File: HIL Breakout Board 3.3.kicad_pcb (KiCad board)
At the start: 4 copper layers, 262.5 x 26.2 mm, 4 parts, among them J1 DIN41612_03x32_C_Split, J2 DIN41612_03x32_C_Split, J3 HDRA-E68W1LFDT1EC+

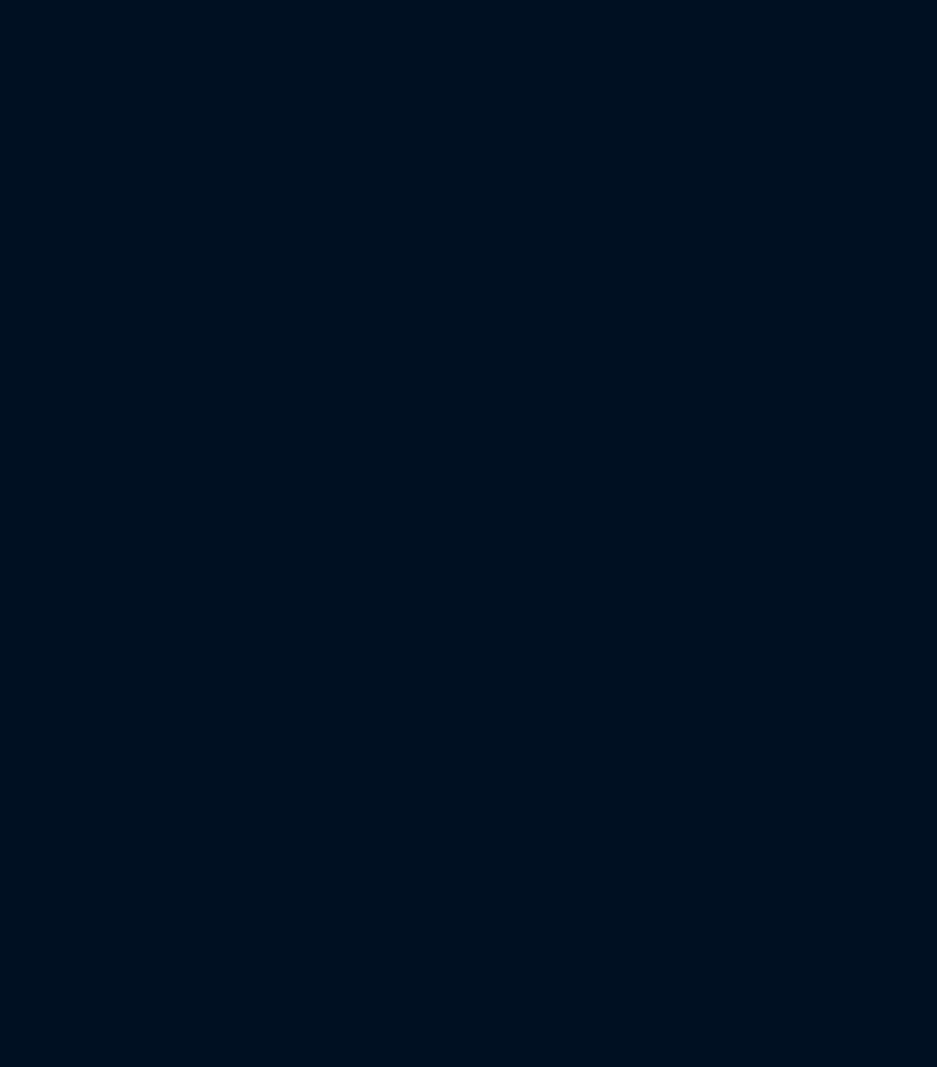
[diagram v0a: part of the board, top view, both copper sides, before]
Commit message: Added all analog inputs and outputs to schematic Schematic still missing +5 V on pin 1 and 35 and AISENSE1 on pin 56 for A and B side Updated PCB Design
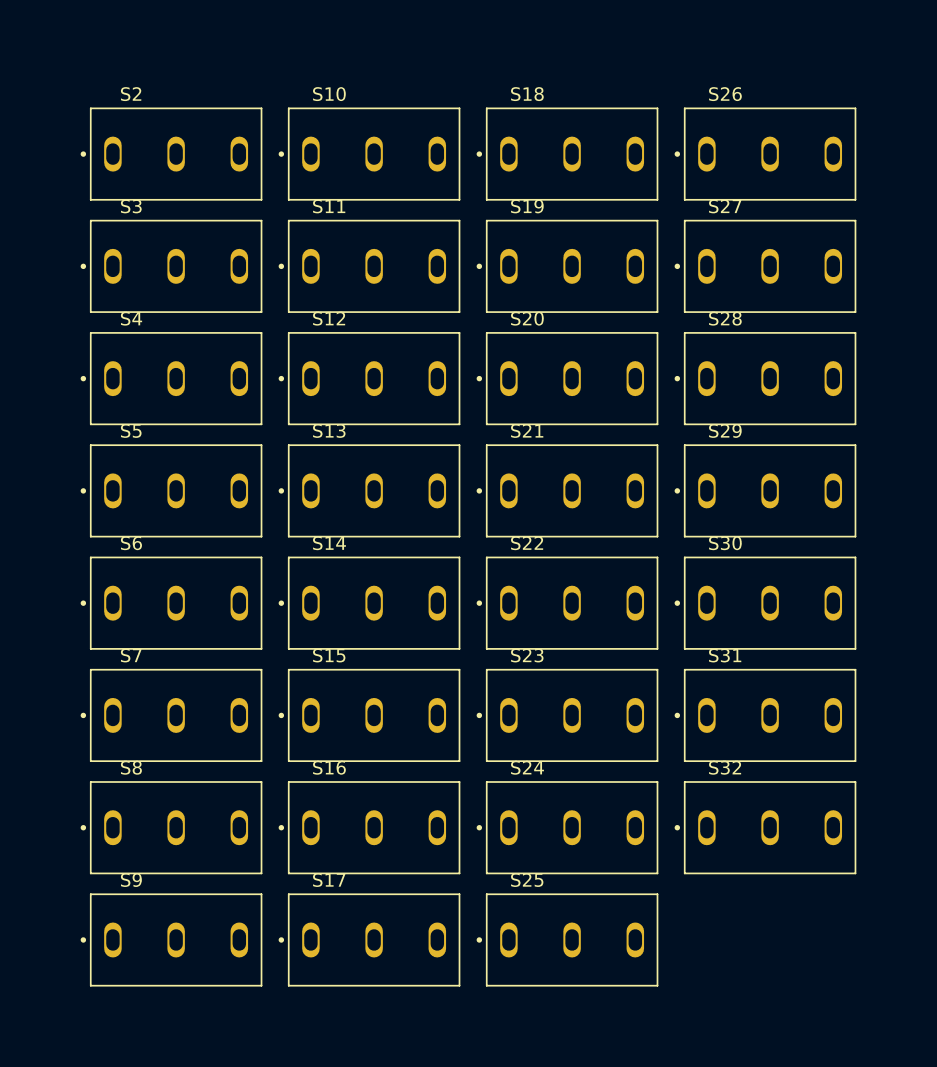
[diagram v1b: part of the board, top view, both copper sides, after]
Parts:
- added S10: SLW-1276864-4A-D, KiCad:SW_SLW-1276864-4A-D, F.Cu at (87.1, 74.3)
- added S11: SLW-1276864-4A-D, KiCad:SW_SLW-1276864-4A-D, F.Cu at (87.1, 82.6)
- added S12: SLW-1276864-4A-D, KiCad:SW_SLW-1276864-4A-D, F.Cu at (87.1, 91.0)
- added S13: SLW-1276864-4A-D, KiCad:SW_SLW-1276864-4A-D, F.Cu at (87.1, 99.3)
- added S14: SLW-1276864-4A-D, KiCad:SW_SLW-1276864-4A-D, F.Cu at (87.1, 107.7)
- added S15: SLW-1276864-4A-D, KiCad:SW_SLW-1276864-4A-D, F.Cu at (87.1, 116.0)
- added S16: SLW-1276864-4A-D, KiCad:SW_SLW-1276864-4A-D, F.Cu at (87.1, 124.4)
- added S17: SLW-1276864-4A-D, KiCad:SW_SLW-1276864-4A-D, F.Cu at (87.1, 132.7)
- added S18: SLW-1276864-4A-D, KiCad:SW_SLW-1276864-4A-D, F.Cu at (101.8, 74.3)
- added S19: SLW-1276864-4A-D, KiCad:SW_SLW-1276864-4A-D, F.Cu at (101.8, 82.6)
- added S2: SLW-1276864-4A-D, KiCad:SW_SLW-1276864-4A-D, F.Cu at (72.4, 74.3)
- added S20: SLW-1276864-4A-D, KiCad:SW_SLW-1276864-4A-D, F.Cu at (101.8, 91.0)
- added S21: SLW-1276864-4A-D, KiCad:SW_SLW-1276864-4A-D, F.Cu at (101.8, 99.3)
- added S22: SLW-1276864-4A-D, KiCad:SW_SLW-1276864-4A-D, F.Cu at (101.8, 107.7)
- added S23: SLW-1276864-4A-D, KiCad:SW_SLW-1276864-4A-D, F.Cu at (101.8, 116.0)
- added S24: SLW-1276864-4A-D, KiCad:SW_SLW-1276864-4A-D, F.Cu at (101.8, 124.4)
- added S25: SLW-1276864-4A-D, KiCad:SW_SLW-1276864-4A-D, F.Cu at (101.8, 132.7)
- added S26: SLW-1276864-4A-D, KiCad:SW_SLW-1276864-4A-D, F.Cu at (116.6, 74.3)
- added S27: SLW-1276864-4A-D, KiCad:SW_SLW-1276864-4A-D, F.Cu at (116.6, 82.6)
- added S28: SLW-1276864-4A-D, KiCad:SW_SLW-1276864-4A-D, F.Cu at (116.6, 91.0)
- added S29: SLW-1276864-4A-D, KiCad:SW_SLW-1276864-4A-D, F.Cu at (116.6, 99.3)
- added S3: SLW-1276864-4A-D, KiCad:SW_SLW-1276864-4A-D, F.Cu at (72.4, 82.6)
- added S30: SLW-1276864-4A-D, KiCad:SW_SLW-1276864-4A-D, F.Cu at (116.6, 107.7)
- added S31: SLW-1276864-4A-D, KiCad:SW_SLW-1276864-4A-D, F.Cu at (116.6, 116.0)
- added S32: SLW-1276864-4A-D, KiCad:SW_SLW-1276864-4A-D, F.Cu at (116.6, 124.4)
- added S4: SLW-1276864-4A-D, KiCad:SW_SLW-1276864-4A-D, F.Cu at (72.4, 91.0)
- added S5: SLW-1276864-4A-D, KiCad:SW_SLW-1276864-4A-D, F.Cu at (72.4, 99.3)
- added S6: SLW-1276864-4A-D, KiCad:SW_SLW-1276864-4A-D, F.Cu at (72.4, 107.7)
- added S7: SLW-1276864-4A-D, KiCad:SW_SLW-1276864-4A-D, F.Cu at (72.4, 116.0)
- added S8: SLW-1276864-4A-D, KiCad:SW_SLW-1276864-4A-D, F.Cu at (72.4, 124.4)
- added S9: SLW-1276864-4A-D, KiCad:SW_SLW-1276864-4A-D, F.Cu at (72.4, 132.7)
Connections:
- net ANO1 renamed AO0
- J1 pad a10: /ANout10 -> AO9
- J1 pad a11: /ANout11 -> AO10
- J1 pad a12: /ANout12 -> AO11
- J1 pad a13: /ANout13 -> AO12
- J1 pad a14: /ANout14 -> AO13
- J1 pad a15: unconnected-(J1A-Pin_a15-Pada15) -> AO14
- J1 pad a16: /ANout16 -> AO15
- J1 pad a2: /ANout2 -> AO1
- J1 pad a25: /ANin1 -> AI0
- J1 pad a26: /ANin2 -> AI1
- J1 pad a27: /ANin3 -> AI2
- J1 pad a28: /ANin4 -> AI3
- J1 pad a29: /ANin5 -> AI4
- J1 pad a3: /ANout3 -> AO2
- J1 pad a30: /ANin6 -> AI5
- J1 pad a31: /ANin7 -> AI6
- J1 pad a32: /ANin8 -> AI7
- J1 pad a4: /ANout4 -> AO3
- J1 pad a5: unconnected-(J1A-Pin_a5-Pada5) -> AO4
- J1 pad a6: /ANout6 -> AO5
- J1 pad a7: /ANout7 -> AO6
- J1 pad a8: /ANout8 -> AO7
- J1 pad a9: /ANout9 -> AO8
- J1 pad b25: /ANin9 -> AI8
- J1 pad b26: /ANin10 -> AI9
- J1 pad b27: /ANin11 -> AI10
- J1 pad b28: /ANin12 -> AI11
- J1 pad b29: /ANin13 -> AI12
- J1 pad b30: /ANin14 -> AI13
- J1 pad b31: /ANin15 -> AI14
- J1 pad b32: /ANin16 -> AI15
- J2 pad a1: /DI1 -> DI0
- J2 pad a10: /DI10 -> DI0
- J2 pad a11: /DI11 -> DI0
- J2 pad a12: /DI12 -> DI0
- J2 pad a13: /DI13 -> DI0
- J2 pad a14: /DI14 -> DI0
- J2 pad a15: /DI15 -> DI0
- J2 pad a16: /DI16 -> DI0
- J2 pad a17: /DI17 -> DI0
- J2 pad a18: /DI18 -> DI0
- J2 pad a19: /DI19 -> DI0
- J2 pad a2: /DI2 -> DI0
- J2 pad a20: /DI20 -> DI0
- J2 pad a21: /DI21 -> DI0
- J2 pad a22: /DI22 -> DI0
- J2 pad a23: /DI23 -> DI0
- J2 pad a24: /DI24 -> DI0
- J2 pad a25: /DI25 -> DI0
- J2 pad a26: /DI26 -> DI0
- J2 pad a27: /DI27 -> DI0
- J2 pad a28: /DI28 -> DI0
- J2 pad a29: /DI29 -> DI0
- J2 pad a3: /DI3 -> DI0
- J2 pad a30: /DI30 -> DI0
- J2 pad a31: /DI31 -> DI0
- J2 pad a32: /DI32 -> DI0
- J2 pad a4: /DI4 -> DI0
- J2 pad a5: /DI5 -> DI0
- J2 pad a6: /DI6 -> DI0
- J2 pad a7: /DI7 -> DI0
- J2 pad a8: /DI8 -> DI0
- J2 pad a9: /DI9 -> DI0
- J2 pad b1: /DO1 -> DO0
- J2 pad b10: /DO10 -> DO0
- J2 pad b11: /DO11 -> DO0
- J2 pad b12: /DO12 -> DO0
- J2 pad b13: /DO13 -> DO0
- J2 pad b14: /DO14 -> DO0
- J2 pad b15: /DO15 -> DO0
- J2 pad b16: /DO16 -> DO0
- J2 pad b17: /DO17 -> DO0
- J2 pad b18: /DO18 -> DO0
- J2 pad b19: /DO19 -> DO0
- J2 pad b2: /DO2 -> DO0
- J2 pad b20: /DO20 -> DO0
- J2 pad b21: /DO21 -> DO0
- J2 pad b22: /DO22 -> DO0
- J2 pad b23: /DO23 -> DO0
- J2 pad b24: /DO24 -> DO0
- J2 pad b25: /DO25 -> DO0
- J2 pad b26: /DO26 -> DO0
- J2 pad b27: /DO27 -> DO0
- J2 pad b28: /DO28 -> DO0
- J2 pad b29: /DO29 -> DO0
- J2 pad b3: /DO3 -> DO0
- J2 pad b30: /DO30 -> DO0
- J2 pad b31: /DO31 -> DO0
- J2 pad b32: /DO32 -> DO0
- J2 pad b4: /DO4 -> DO0
- J2 pad b5: /DO5 -> DO0
- J2 pad b6: /DO6 -> DO0
- J2 pad b7: /DO7 -> DO0
- J2 pad b8: /DO8 -> DO0
- J2 pad b9: /DO9 -> DO0
- J3 pad A10: unconnected-(J3-PadA10) -> Net-(J3-PadA10)
- J3 pad A11: unconnected-(J3-PadA11) -> Net-(J3-PadA11)
- J3 pad A12: unconnected-(J3-PadA12) -> Net-(J3-PadA12)
- J3 pad A13: unconnected-(J3-PadA13) -> Net-(J3-PadA13)
- J3 pad A14: unconnected-(J3-PadA14) -> AGND
- J3 pad A15: unconnected-(J3-PadA15) -> AGND
- J3 pad A16: unconnected-(J3-PadA16) -> AGND
- J3 pad A17: unconnected-(J3-PadA17) -> AGND
- J3 pad A18: unconnected-(J3-PadA18) -> AGND
- J3 pad A19: unconnected-(J3-PadA19) -> AGND
- J3 pad A2: unconnected-(J3-PadA2) -> DGND
- J3 pad A20: unconnected-(J3-PadA20) -> AGND
- J3 pad A21: unconnected-(J3-PadA21) -> AGND
- J3 pad A24: unconnected-(J3-PadA24) -> AGND
- J3 pad A27: unconnected-(J3-PadA27) -> AGND
- J3 pad A3: unconnected-(J3-PadA3) -> DGND
- J3 pad A30: unconnected-(J3-PadA30) -> AGND
- J3 pad A33: unconnected-(J3-PadA33) -> AGND
- J3 pad A37: unconnected-(J3-PadA37) -> Net-(J3-PadA37)
- J3 pad A38: unconnected-(J3-PadA38) -> Net-(J3-PadA38)
- J3 pad A39: unconnected-(J3-PadA39) -> Net-(J3-PadA39)
- J3 pad A4: unconnected-(J3-PadA4) -> DGND
- J3 pad A40: unconnected-(J3-PadA40) -> Net-(J3-PadA40)
- J3 pad A41: unconnected-(J3-PadA41) -> Net-(J3-PadA41)
- J3 pad A42: unconnected-(J3-PadA42) -> Net-(J3-PadA42)
- J3 pad A43: unconnected-(J3-PadA43) -> Net-(J3-PadA43)
- J3 pad A44: unconnected-(J3-PadA44) -> Net-(J3-PadA44)
- J3 pad A45: unconnected-(J3-PadA45) -> Net-(J3-PadA45)
- J3 pad A46: unconnected-(J3-PadA46) -> Net-(J3-PadA46)
- J3 pad A47: unconnected-(J3-PadA47) -> Net-(J3-PadA47)
- J3 pad A48: unconnected-(J3-PadA48) -> AI7
- J3 pad A49: unconnected-(J3-PadA49) -> AI6
- J3 pad A5: unconnected-(J3-PadA5) -> DGND
- J3 pad A50: unconnected-(J3-PadA50) -> AI5
- J3 pad A51: unconnected-(J3-PadA51) -> AI4
- J3 pad A52: unconnected-(J3-PadA52) -> AI3
- J3 pad A53: unconnected-(J3-PadA53) -> AI2
- J3 pad A54: unconnected-(J3-PadA54) -> AI1
- J3 pad A55: unconnected-(J3-PadA55) -> AI0
- J3 pad A57: unconnected-(J3-PadA57) -> AO7
- J3 pad A58: unconnected-(J3-PadA58) -> AGND
- J3 pad A59: unconnected-(J3-PadA59) -> AO6
- J3 pad A6: unconnected-(J3-PadA6) -> DGND
- J3 pad A60: unconnected-(J3-PadA60) -> AO5
- J3 pad A61: unconnected-(J3-PadA61) -> AGND
- J3 pad A62: unconnected-(J3-PadA62) -> AO4
- J3 pad A63: unconnected-(J3-PadA63) -> AO3
- J3 pad A64: unconnected-(J3-PadA64) -> AGND
- J3 pad A65: unconnected-(J3-PadA65) -> AO2
- J3 pad A66: unconnected-(J3-PadA66) -> AO1
- J3 pad A7: unconnected-(J3-PadA7) -> DGND
- J3 pad A8: unconnected-(J3-PadA8) -> DGND
- J3 pad A9: unconnected-(J3-PadA9) -> DGND
- J3 pad B10: unconnected-(J3-PadB10) -> Net-(J3-PadB10)
- J3 pad B11: unconnected-(J3-PadB11) -> Net-(J3-PadB11)
- J3 pad B12: unconnected-(J3-PadB12) -> Net-(J3-PadB12)
- J3 pad B13: unconnected-(J3-PadB13) -> Net-(J3-PadB13)
- J3 pad B14: unconnected-(J3-PadB14) -> AGND
- J3 pad B15: unconnected-(J3-PadB15) -> AGND
- J3 pad B16: unconnected-(J3-PadB16) -> AGND
- J3 pad B17: unconnected-(J3-PadB17) -> AGND
- J3 pad B18: unconnected-(J3-PadB18) -> AGND
- J3 pad B19: unconnected-(J3-PadB19) -> AGND
- J3 pad B2: unconnected-(J3-PadB2) -> DGND
- J3 pad B20: unconnected-(J3-PadB20) -> AGND
- J3 pad B21: unconnected-(J3-PadB21) -> AGND
- J3 pad B24: unconnected-(J3-PadB24) -> AGND
- J3 pad B27: unconnected-(J3-PadB27) -> AGND
- J3 pad B3: unconnected-(J3-PadB3) -> DGND
- J3 pad B30: unconnected-(J3-PadB30) -> AGND
- J3 pad B33: unconnected-(J3-PadB33) -> AGND
- J3 pad B36: unconnected-(J3-PadB36) -> Net-(J3-PadB36)
- J3 pad B37: unconnected-(J3-PadB37) -> Net-(J3-PadB37)
- J3 pad B38: unconnected-(J3-PadB38) -> Net-(J3-PadB38)
- J3 pad B39: unconnected-(J3-PadB39) -> Net-(J3-PadB39)
- J3 pad B4: unconnected-(J3-PadB4) -> DGND
- J3 pad B40: unconnected-(J3-PadB40) -> Net-(J3-PadB40)
- J3 pad B41: unconnected-(J3-PadB41) -> Net-(J3-PadB41)
- J3 pad B42: unconnected-(J3-PadB42) -> Net-(J3-PadB42)
- J3 pad B43: unconnected-(J3-PadB43) -> Net-(J3-PadB43)
- J3 pad B44: unconnected-(J3-PadB44) -> Net-(J3-PadB44)
- J3 pad B45: unconnected-(J3-PadB45) -> Net-(J3-PadB45)
- J3 pad B46: unconnected-(J3-PadB46) -> Net-(J3-PadB46)
- J3 pad B47: unconnected-(J3-PadB47) -> Net-(J3-PadB47)
- J3 pad B48: unconnected-(J3-PadB48) -> AI15
- J3 pad B49: unconnected-(J3-PadB49) -> AI14
- J3 pad B5: unconnected-(J3-PadB5) -> DGND
- J3 pad B50: unconnected-(J3-PadB50) -> AI13
- J3 pad B51: unconnected-(J3-PadB51) -> AI12
- J3 pad B52: unconnected-(J3-PadB52) -> AI11
- J3 pad B53: unconnected-(J3-PadB53) -> AI10
- J3 pad B54: unconnected-(J3-PadB54) -> AI9
- J3 pad B55: unconnected-(J3-PadB55) -> AI8
- J3 pad B57: unconnected-(J3-PadB57) -> AO15
- J3 pad B58: unconnected-(J3-PadB58) -> AGND
- J3 pad B59: unconnected-(J3-PadB59) -> AO14
- J3 pad B6: unconnected-(J3-PadB6) -> DGND
- J3 pad B60: unconnected-(J3-PadB60) -> AO13
- J3 pad B61: unconnected-(J3-PadB61) -> AGND
- J3 pad B62: unconnected-(J3-PadB62) -> AO12
- J3 pad B63: unconnected-(J3-PadB63) -> AO11
- J3 pad B64: unconnected-(J3-PadB64) -> AGND
- J3 pad B65: unconnected-(J3-PadB65) -> AO10
- J3 pad B66: unconnected-(J3-PadB66) -> AO9
- J3 pad B67: unconnected-(J3-PadB67) -> AGND
- J3 pad B68: unconnected-(J3-PadB68) -> AO8
- J3 pad B7: unconnected-(J3-PadB7) -> DGND
- J3 pad B8: unconnected-(J3-PadB8) -> DGND
- J3 pad B9: unconnected-(J3-PadB9) -> DGND
- S1 pad 1: /DI1 -> DI0
- S1 pad 3: /DO1 -> DO0

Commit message: Fixed the issue with naming of net labels so that all digital pins were not tied together
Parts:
- moved S32 162.0 mm to (277.9, 109.1), turned to 90 degrees
- moved S31 153.1 mm to (269.5, 109.1), turned to 90 degrees
- moved S30 144.6 mm to (261.2, 109.1), turned to 90 degrees
- moved S29 136.6 mm to (252.8, 109.1), turned to 90 degrees
- moved S28 129.2 mm to (244.5, 109.1), turned to 90 degrees
- moved S1 124.1 mm to (20.3, 109.1)
- moved S27 122.4 mm to (236.1, 109.1), turned to 90 degrees
- moved S25 120.2 mm to (219.7, 109.1), turned to 90 degrees
- moved S26 116.5 mm to (227.8, 109.1), turned to 90 degrees
- moved S24 110.6 mm to (211.4, 109.1), turned to 90 degrees
- moved S23 101.4 mm to (203.0, 109.1), turned to 90 degrees
- moved S22 92.8 mm to (194.7, 109.1), turned to 90 degrees
- moved S21 85.0 mm to (186.3, 109.1), turned to 90 degrees
- moved S20 78.2 mm to (178.0, 109.1), turned to 90 degrees
- moved S19 72.8 mm to (169.6, 109.1), turned to 90 degrees
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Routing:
- net AO0: track 222.5 -> 0.00 mm, vias 2 -> 0

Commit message: Got rid of all names of wires because it was causing issues with global variables Started PCB tracks
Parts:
- moved S1 169.0 mm to (184.8, 70.4), turned to 0 degrees
- moved S2 159.1 mm to (184.8, 80.5), turned to 0 degrees
- moved S3 149.3 mm to (184.8, 90.7), turned to 0 degrees
- moved S4 140.0 mm to (184.8, 100.8), turned to 0 degrees
- moved S5 131.5 mm to (184.8, 111.0), turned to 0 degrees
- moved S9 124.5 mm to (205.0, 70.4), turned to 0 degrees
- moved S6 123.7 mm to (184.8, 121.1), turned to 0 degrees
- moved S7 116.9 mm to (184.8, 131.2), turned to 0 degrees
- moved S10 113.9 mm to (205.1, 80.5), turned to 0 degrees
- moved S8 111.2 mm to (184.8, 141.4), turned to 0 degrees
- moved S11 103.6 mm to (205.1, 90.7), turned to 0 degrees
- moved S12 93.9 mm to (205.1, 100.8), turned to 0 degrees
- moved S13 85.2 mm to (205.0, 111.0), turned to 0 degrees
- moved S17 82.1 mm to (225.8, 70.4), turned to 0 degrees
- moved S14 78.0 mm to (205.2, 121.1), turned to 0 degrees
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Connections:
- J2 pad a10: DI0 -> DI9
- J2 pad a11: DI0 -> DI10
- J2 pad a12: DI0 -> DI11
- J2 pad a13: DI0 -> DI12
- J2 pad a14: DI0 -> DI13
- J2 pad a15: DI0 -> DI14
- J2 pad a16: DI0 -> DI15
- J2 pad a17: DI0 -> DI16
- J2 pad a18: DI0 -> DI17
- J2 pad a19: DI0 -> DI18
- J2 pad a2: DI0 -> DI1
- J2 pad a20: DI0 -> DI19
- J2 pad a21: DI0 -> DI20
- J2 pad a22: DI0 -> DI21
- J2 pad a23: DI0 -> DI22
- J2 pad a24: DI0 -> DI23
- J2 pad a25: DI0 -> DI24
- J2 pad a26: DI0 -> DI25
- J2 pad a27: DI0 -> DI26
- J2 pad a28: DI0 -> DI27
- J2 pad a29: DI0 -> DI28
- J2 pad a3: DI0 -> DI2
- J2 pad a30: DI0 -> DI29
- J2 pad a31: DI0 -> DI30
- J2 pad a32: DI0 -> DI31
- J2 pad a4: DI0 -> DI3
- J2 pad a5: DI0 -> DI4
- J2 pad a6: DI0 -> DI5
- J2 pad a7: DI0 -> DI6
- J2 pad a8: DI0 -> DI7
- J2 pad a9: DI0 -> DI8
- J2 pad b10: DO0 -> DO9
- J2 pad b11: DO0 -> DO10
- J2 pad b12: DO0 -> DO11
- J2 pad b13: DO0 -> DO12
- J2 pad b14: DO0 -> DO13
- J2 pad b15: DO0 -> DO14
- J2 pad b16: DO0 -> DO15
- J2 pad b17: DO0 -> DO16
- J2 pad b18: DO0 -> DO17
- J2 pad b19: DO0 -> DO18
- J2 pad b2: DO0 -> DO1
- J2 pad b20: DO0 -> DO19
- J2 pad b21: DO0 -> DO20
- J2 pad b22: DO0 -> DO21
- J2 pad b23: DO0 -> DO22
- J2 pad b24: DO0 -> DO23
- J2 pad b25: DO0 -> DO24
- J2 pad b26: DO0 -> DO25
- J2 pad b27: DO0 -> DO26
- J2 pad b28: DO0 -> DO27
- J2 pad b29: DO0 -> DO28
- J2 pad b3: DO0 -> DO2
- J2 pad b30: DO0 -> DO29
- J2 pad b31: DO0 -> DO30
- J2 pad b32: DO0 -> DO31
- J2 pad b4: DO0 -> DO3
- J2 pad b5: DO0 -> DO4
- J2 pad b6: DO0 -> DO5
- J2 pad b7: DO0 -> DO6
- J2 pad b8: DO0 -> DO7
- J2 pad b9: DO0 -> DO8
- S10 pad 1: DI0 -> DI9
- S10 pad 3: DO0 -> DO9
- S11 pad 1: DI0 -> DI10
- S11 pad 3: DO0 -> DO10
- S12 pad 1: DI0 -> DI11
- S12 pad 3: DO0 -> DO11
- S13 pad 1: DI0 -> DI12
- S13 pad 3: DO0 -> DO12
- S14 pad 1: DI0 -> DI13
- S14 pad 3: DO0 -> DO13
- S15 pad 1: DI0 -> DI14
- S15 pad 3: DO0 -> DO14
- S16 pad 1: DI0 -> DI15
- S16 pad 3: DO0 -> DO15
- S17 pad 1: DI0 -> DI16
- S17 pad 3: DO0 -> DO16
- S18 pad 1: DI0 -> DI17
- S18 pad 3: DO0 -> DO17
- S19 pad 1: DI0 -> DI18
- S19 pad 3: DO0 -> DO18
- S2 pad 1: DI0 -> DI1
- S2 pad 3: DO0 -> DO1
- S20 pad 1: DI0 -> DI19
- S20 pad 3: DO0 -> DO19
- S21 pad 1: DI0 -> DI20
- S21 pad 3: DO0 -> DO20
- S22 pad 1: DI0 -> DI21
- S22 pad 3: DO0 -> DO21
- S23 pad 1: DI0 -> DI22
- S23 pad 3: DO0 -> DO22
- S24 pad 1: DI0 -> DI23
- S24 pad 3: DO0 -> DO23
- S25 pad 1: DI0 -> DI24
- S25 pad 3: DO0 -> DO24
- S26 pad 1: DI0 -> DI25
- S26 pad 3: DO0 -> DO25
- S27 pad 1: DI0 -> DI26
- S27 pad 3: DO0 -> DO26
- S28 pad 1: DI0 -> DI27
- S28 pad 3: DO0 -> DO27
- S29 pad 1: DI0 -> DI28
- S29 pad 3: DO0 -> DO28
- S3 pad 1: DI0 -> DI2
- S3 pad 3: DO0 -> DO2
- S30 pad 1: DI0 -> DI29
- S30 pad 3: DO0 -> DO29
- S31 pad 1: DI0 -> DI30
- S31 pad 3: DO0 -> DO30
- S32 pad 1: DI0 -> DI31
- S32 pad 3: DO0 -> DO31
- S4 pad 1: DI0 -> DI3
- S4 pad 3: DO0 -> DO3
- S5 pad 1: DI0 -> DI4
- S5 pad 3: DO0 -> DO4
- S6 pad 1: DI0 -> DI5
- S6 pad 3: DO0 -> DO5
- S7 pad 1: DI0 -> DI6
- S7 pad 3: DO0 -> DO6
- S8 pad 1: DI0 -> DI7
- S8 pad 3: DO0 -> DO7
- S9 pad 1: DI0 -> DI8
- S9 pad 3: DO0 -> DO8
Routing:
- net AO0: track 0.00 -> 107.5 mm, vias 0 -> 3
- net AO1: track 0.00 -> 102.9 mm, vias 0 -> 2
- net AO2: track 0.00 -> 99.8 mm, vias 0 -> 2
- net AO3: track 0.00 -> 95.8 mm, vias 0 -> 2
- net AO4: track 0.00 -> 91.4 mm, vias 0 -> 2
- net AO5: track 0.00 -> 88.1 mm, vias 0 -> 2
- net AO6: track 0.00 -> 85.4 mm, vias 0 -> 2
- net AI4: track 0.00 -> 83.7 mm, vias 0 -> 2
- net AO7: track 0.00 -> 82.5 mm, vias 0 -> 2
- net AI3: track 0.00 -> 79.2 mm, vias 0 -> 2
- net AI2: track 0.00 -> 76.6 mm, vias 0 -> 2
- net AI1: track 0.00 -> 71.3 mm, vias 0 -> 2
- net AI0: track 0.00 -> 69.1 mm, vias 0 -> 2

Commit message: Added all analog traces Changed NI connection to two separate ports Added footprint folders for switch and NI connector
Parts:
- removed J3: HDRA-E68W1LFDT1EC+, KiCad:HDRAE68W1LFDT1EC
- added J4: 2-5174225-5, ProjectSpecificFootprints:TE_2-5174225-5, F.Cu at (80.1, 142.7)
- added J5: 2-5174225-5, ProjectSpecificFootprints:TE_2-5174225-5, F.Cu at (209.5, 142.7)
- S1, S10, S11, S12, S13, S14, S15, S16, S17, S18, S19, S2, S20, S21, S22, S23, S24, S25, S26, S27, S28, S29, S3, S30, S31, S32, S4, S5, S6, S7, S8, S9: footprint KiCad:SW_SLW-1276864-4A-D -> ProjectSpecificFootprints:SW_SLW-1276864-4A-D
- moved S17 162.2 mm to (67.1, 103.6), turned to 90 degrees
- moved S18 150.4 mm to (77.3, 103.6), turned to 90 degrees
- moved S19 138.9 mm to (87.5, 103.6), turned to 90 degrees
- moved S20 128.1 mm to (97.8, 103.6), turned to 90 degrees
- moved S21 118.1 mm to (108.0, 103.6), turned to 90 degrees
- moved S1 118.1 mm to (67.1, 80.5), turned to 90 degrees
- moved S22 109.0 mm to (118.3, 103.6), turned to 90 degrees
- moved S2 107.5 mm to (77.3, 80.5), turned to 90 degrees
- moved S25 102.8 mm to (149.0, 103.6), turned to 90 degrees
- moved S23 101.3 mm to (128.5, 103.6), turned to 90 degrees
- moved S3 97.8 mm to (87.5, 80.5), turned to 90 degrees
- moved S24 94.9 mm to (138.7, 103.6), turned to 90 degrees
- moved S26 90.0 mm to (159.2, 103.6), turned to 90 degrees
- moved S4 89.3 mm to (97.8, 80.5), turned to 90 degrees
- moved S5 82.6 mm to (108.0, 80.5), turned to 90 degrees
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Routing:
- net +5Vout: track 0.00 -> 303.5 mm, vias 0 -> 3
- net AO13: track 0.00 -> 276.0 mm, vias 0 -> 2
- net AO11: track 0.00 -> 275.5 mm, vias 0 -> 2
- net AO12: track 0.00 -> 274.3 mm, vias 0 -> 2
- net AO9: track 0.00 -> 272.5 mm, vias 0 -> 2
- net AO8: track 0.00 -> 268.4 mm, vias 0 -> 2
- net AO10: track 0.00 -> 262.2 mm, vias 0 -> 2
- net AO14: track 0.00 -> 256.9 mm, vias 0 -> 2
- net AO15: track 0.00 -> 255.2 mm, vias 0 -> 2
- net AI8: track 0.00 -> 210.5 mm
- net AI9: track 0.00 -> 206.5 mm, vias 0 -> 2
- net AI11: track 0.00 -> 192.4 mm, vias 0 -> 1
- net AI10: track 0.00 -> 191.9 mm, vias 0 -> 1
- net AI5: track 0.00 -> 190.7 mm, vias 0 -> 2
- net AI6: track 0.00 -> 190.0 mm, vias 0 -> 2
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- added copper zone on In2.Cu, net AGND
- added copper zone on In3.Cu, net DGND
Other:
- board size 262.5 x 26.2 mm -> 262.5 x 110.1 mm
- copper layers 4 -> 6
- board text added: "NI Digital Control"
- board text added: "NI Input"
- board text added: "NI Output"
